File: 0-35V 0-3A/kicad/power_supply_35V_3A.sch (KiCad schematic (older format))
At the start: 10 parts, among them J1 220VAC

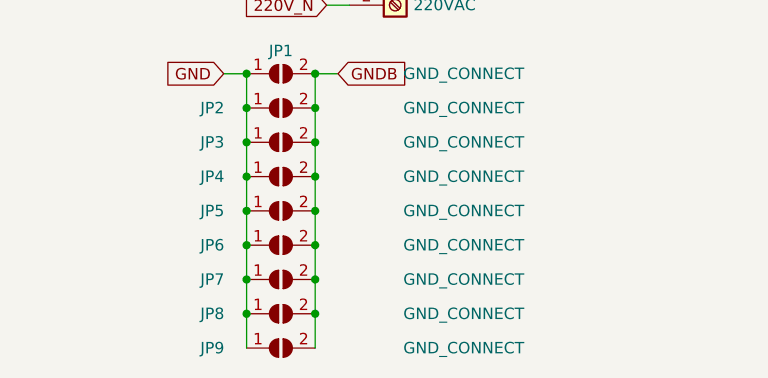
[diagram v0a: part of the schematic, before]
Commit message: Fix PCB ground planes
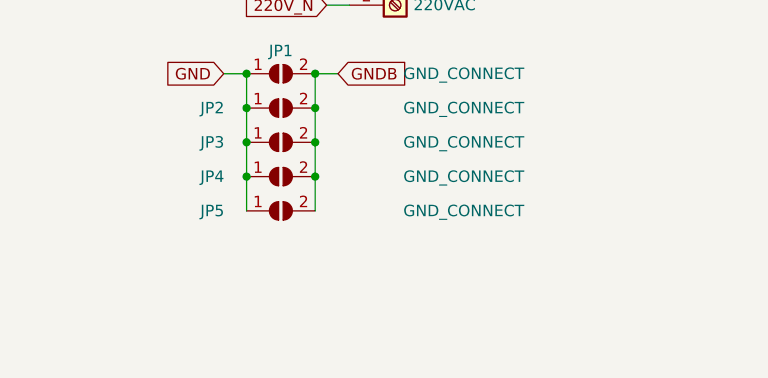
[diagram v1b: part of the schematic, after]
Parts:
- removed JP6, JP7, JP8, JP9: GND_CONNECT, Jumper:SolderJumper-2_P1.3mm_Open_Pad1.0x1.5mm, symbol Jumper:SolderJumper_2_Open
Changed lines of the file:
@@
 	4650 5950 4650 5800
 Connection ~ 4650 5800
-$Comp
-L Jumper:SolderJumper_2_Open JP6
-U 1 1 5F9C9F5B
-P 4500 6100
-F 0 "JP6" H 4200 6100 50  0000 C CNN
-F 1 "GND_CONNECT" H 5300 6100 50  0000 C CNN
-F 2 "Jumper:SolderJumper-2_P1.3mm_Open_Pad1.0x1.5mm" H 4500 6100 50  0001 C CNN
-F 3 "~" H 4500 6100 50  0001 C CNN
-	1    4500 6100
-	1    0    0    -1
-$EndComp
-$Comp
-L Jumper:SolderJumper_2_Open JP7
-U 1 1 5F9CA1E4
-P 4500 6250
-F 0 "JP7" H 4200 6250 50  0000 C CNN
-F 1 "GND_CONNECT" H 5300 6250 50  0000 C CNN
-F 2 "Jumper:SolderJumper-2_P1.3mm_Open_Pad1.0x1.5mm" H 4500 6250 50  0001 C CNN
-F 3 "~" H 4500 6250 50  0001 C CNN
-	1    4500 6250
-	1    0    0    -1
-$EndComp
-$Comp
-L Jumper:SolderJumper_2_Open JP8
-U 1 1 5F9CA3E9
-P 4500 6400
-F 0 "JP8" H 4200 6400 50  0000 C CNN
-F 1 "GND_CONNECT" H 5300 6400 50  0000 C CNN
-F 2 "Jumper:SolderJumper-2_P1.3mm_Open_Pad1.0x1.5mm" H 4500 6400 50  0001 C CNN
-F 3 "~" H 4500 6400 50  0001 C CNN
-	1    4500 6400
-	1    0    0    -1
-$EndComp
-$Comp
-L Jumper:SolderJumper_2_Open JP9
-U 1 1 5F9CA5B7
-P 4500 6550
-F 0 "JP9" H 4200 6550 50  0000 C CNN
-F 1 "GND_CONNECT" H 5300 6550 50  0000 C CNN
-F 2 "Jumper:SolderJumper-2_P1.3mm_Open_Pad1.0x1.5mm" H 4500 6550 50  0001 C CNN
-F 3 "~" H 4500 6550 50  0001 C CNN
-	1    4500 6550
-	1    0    0    -1
-$EndComp
-Connection ~ 4350 6100
-Wire Wire Line
-	4350 6100 4350 6250
-Connection ~ 4350 6250
-Wire Wire Line
-	4350 6250 4350 6400
-Connection ~ 4350 6400
-Wire Wire Line
-	4350 6400 4350 6550
-Wire Wire Line
-	4350 5950 4350 6100
-Connection ~ 4350 5950
-Wire Wire Line
-	4650 6550 4650 6400
-Connection ~ 4650 5950
-Connection ~ 4650 6100
-Wire Wire Line
-	4650 6100 4650 5950
-Connection ~ 4650 6250
-Wire Wire Line
-	4650 6250 4650 6100
-Connection ~ 4650 6400
-Wire Wire Line
-	4650 6400 4650 6250
 $EndSCHEMATC
